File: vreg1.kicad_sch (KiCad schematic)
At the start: 24 parts, among them J1 Conn_01x02, J2 Conn_01x02, Q1 BC817, Q2 DMG2301L, U1 L7805

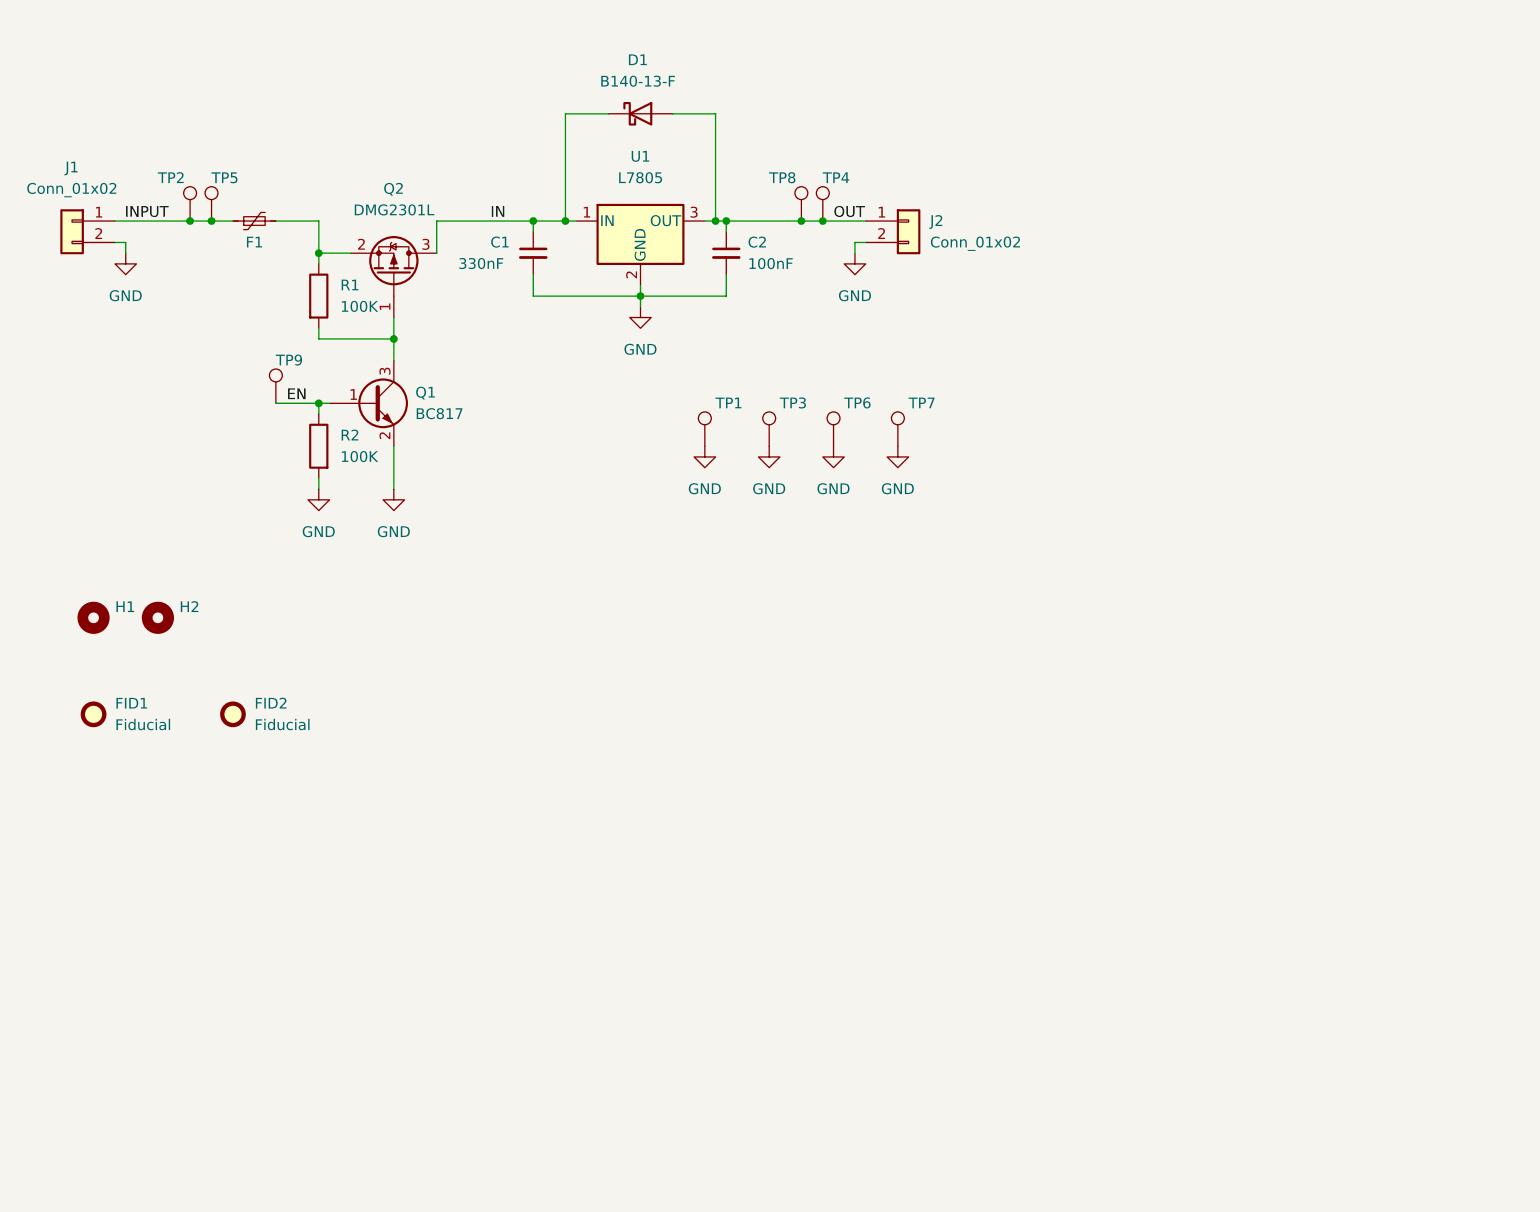
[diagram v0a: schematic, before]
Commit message: Add logotype, move GND TP to right side
Add PDFs for schematics and BOM
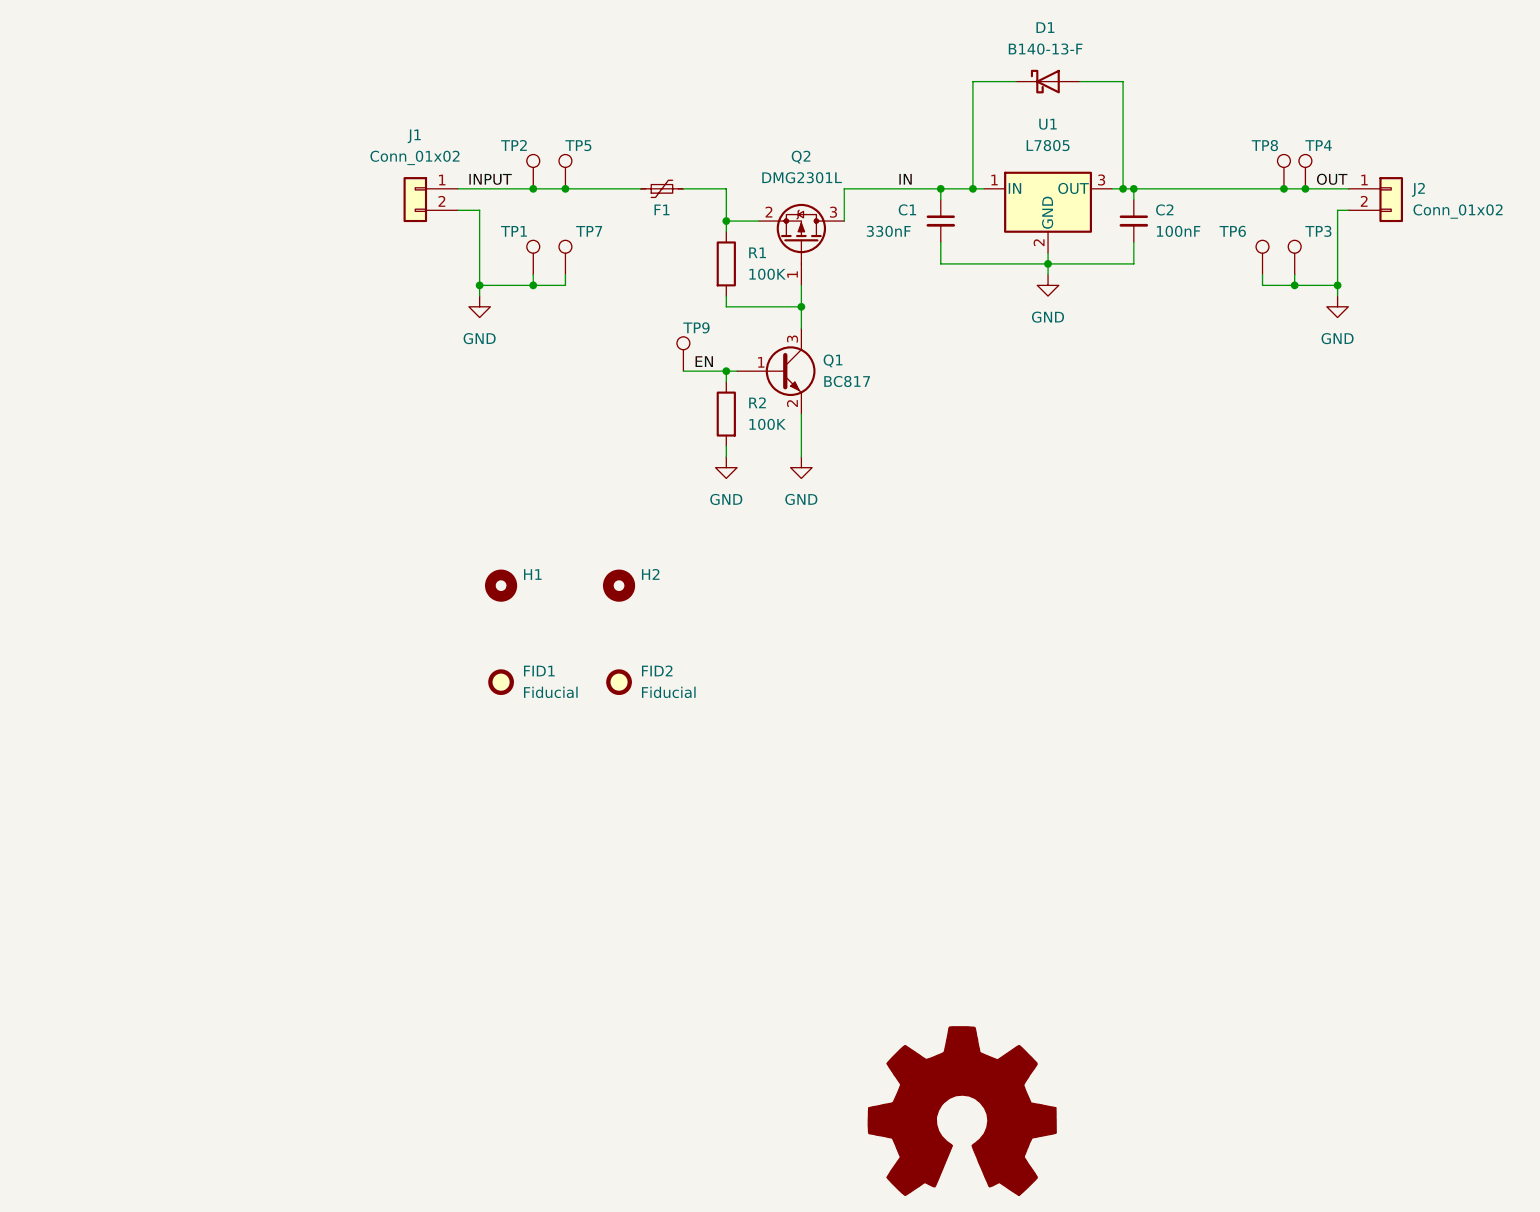
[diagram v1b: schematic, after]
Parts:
- C1: MFP (none) -> CC1206KRX7R9BB334
- C2: MFP (none) -> CC0603KRX7R9BB104
- D1: MFP (none) -> B140-13-F
- F1: MFP (none) -> JK-NSMD025-30V
- FID1, FID2: now left out of the parts list
- Q1: MFP (none) -> BC817-25,215
- Q2: MFP (none) -> DMG2301U-7
- R1, R2: MFP (none) -> 0603WAF1003T5E
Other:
- company: (none) -> E2 Labs
- title: (none) -> Voltage regulator LM7805
- moved on the sheet: C1, C2, D1, F1, FID1, FID2, H1, H2, J1, J2, Q1, Q2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
